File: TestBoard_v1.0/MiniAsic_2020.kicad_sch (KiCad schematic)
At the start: 28 parts, among them J1 Screw_Terminal_01x04, J2 Conn_Coaxial, J3 Conn_Coaxial, J4 Conn_Coaxial, J5 Conn_Coaxial, T1 50@900MHz, T2 50@900MHz, T3 50@900MHz

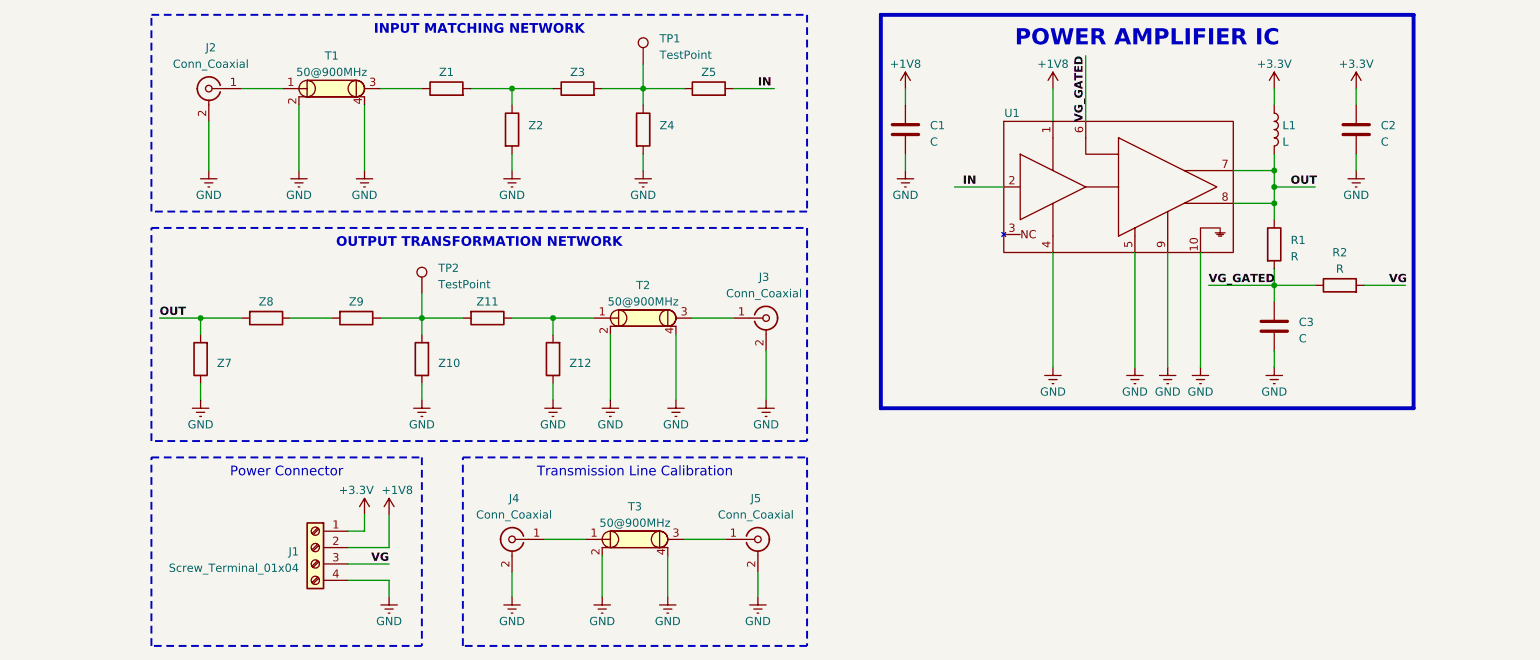
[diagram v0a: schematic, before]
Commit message: Schematic update and initial placement
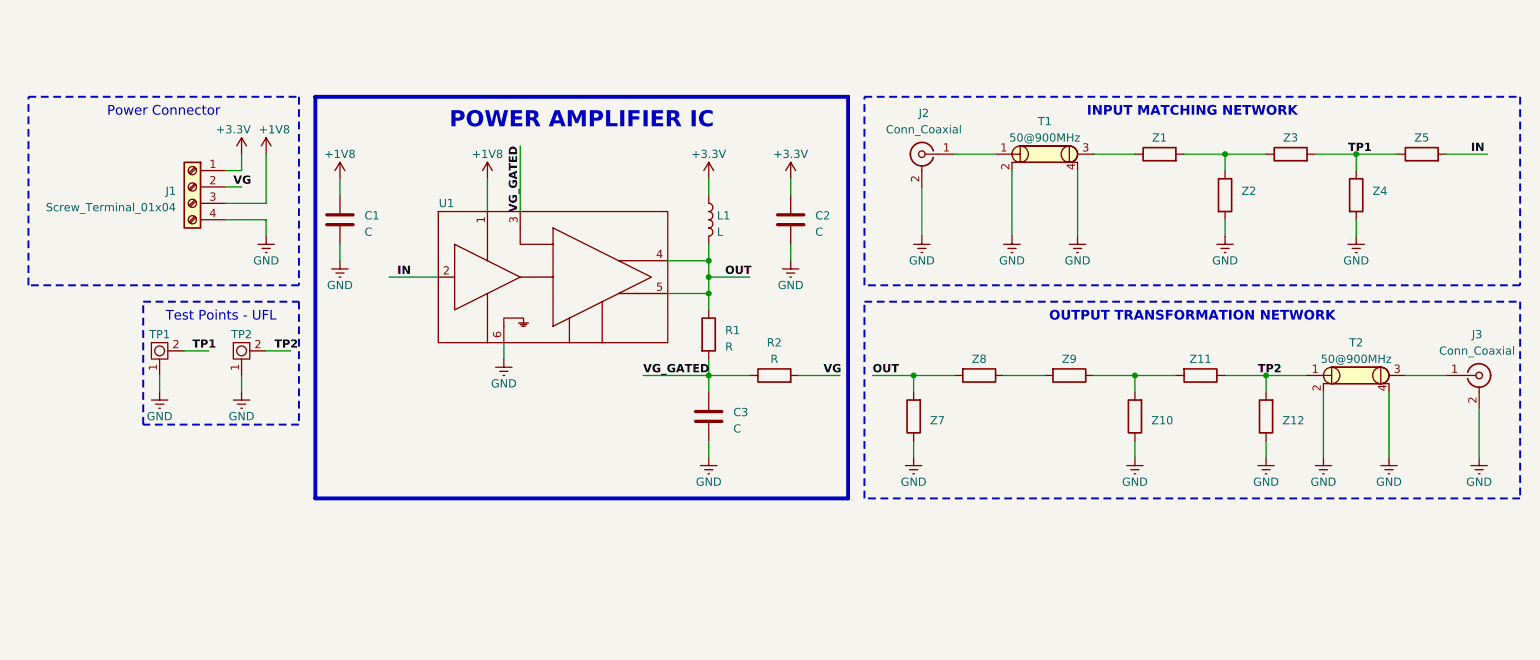
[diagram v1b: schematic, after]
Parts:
- removed J4, J5: Conn_Coaxial, Connector_Coaxial:SMA_Amphenol_901-143_Horizontal, symbol Connector:Conn_Coaxial
- removed T3: 50@900MHz, symbol Simulation_SPICE:TLINE
- removed TP1, TP2: TestPoint, Connector_Coaxial:U.FL_Hirose_U.FL-R-SMT-1_Vertical, symbol Connector:TestPoint
- added TP1, TP2: ~, Connector_Coaxial:U.FL_Hirose_U.FL-R-SMT-1_Vertical, symbol MiniAsic2020_Library_Symbol:TestPoint_UFL
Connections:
- net +1V8: now also J1.3 (Pin_3); no longer J1.2 (Pin_2)
- net OUT: now also U1.4 (OUT_1), U1.5 (OUT_2); no longer U1.7 (OUT_1), U1.8 (OUT_2)
- net VG: now also J1.2 (Pin_2); no longer J1.3 (Pin_3)
- net VG_GATED: now also U1.3 (VG); no longer U1.6 (VG)
- net TP1: now reaches Z3.2, Z4.1, Z5.1
- net TP1: now also TP1.2 (PRB)
- net TP2: now reaches T2.1, Z11.1, Z12.2
- net TP2: now also TP2.2 (PRB)
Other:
- moved on the sheet: C1, C2, C3, J1, J2, J3, L1, R1, R2, T1, T2, Z1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

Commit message: Initial routing
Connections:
- net TP1: now also TP1.1 (PRB); no longer TP1.2 (PRB)
- net TP2: now also TP2.1 (PRB), Z10.2, Z11.2, Z9.1; no longer T2.1, TP2.2 (PRB), Z11.1, Z12.2
- new net: T2.1, Z11.1, Z12.2
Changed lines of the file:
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@@
     (effects (font (size 1.27 1.27) (thickness 0.254) bold) (justify left bottom))
-  )
-  (label "TP2" (at 222.25 106.68 0) (fields_autoplaced)
-    (effects (font (size 1.27 1.27) bold) (justify left bottom))
   )
   (label "TP1" (at 236.22 72.39 0) (fields_autoplaced)
@@
   (label "VG" (at 63.5 77.47 0) (fields_autoplaced)
     (effects (font (size 1.27 1.27) bold) (justify left bottom))
+  )
+  (label "TP2" (at 201.93 106.68 0) (fields_autoplaced)
+    (effects (font (size 1.27 1.27) (thickness 0.254) bold) (justify left bottom))
   )
   (label "IN" (at 255.27 72.39 0) (fields_autoplaced)
@@
     )
   )
-  (symbol (lib_id "MiniAsic2020_Library_Symbol:TestPoint_UFL") (at 52.07 106.68 0) (unit 1)
+  (symbol (lib_name "TestPoint_UFL_1") (lib_id "MiniAsic2020_Library_Symbol:TestPoint_UFL") (at 52.07 106.68 0) (unit 1)
     (in_bom yes) (on_board yes) (dnp no) (fields_autoplaced)
     (property "Reference" "TP1" (at 52.07 100.33 0)

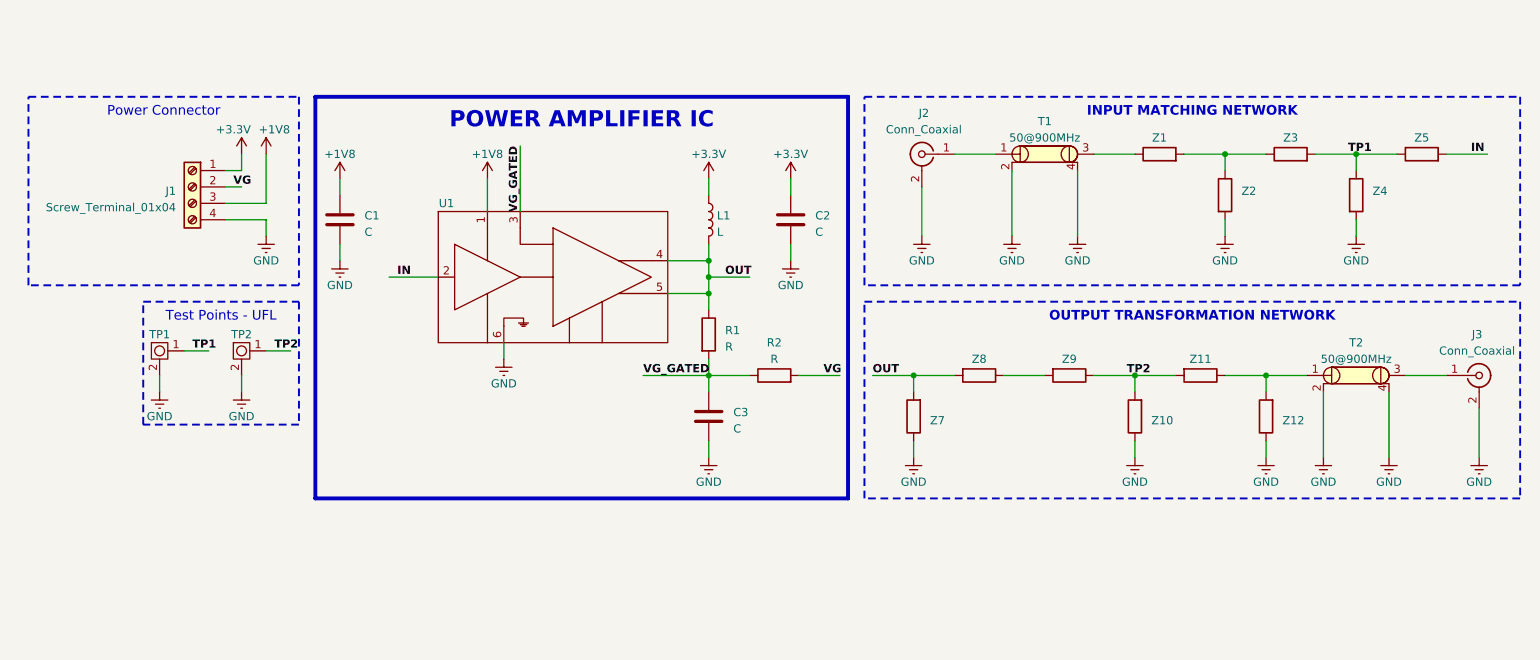
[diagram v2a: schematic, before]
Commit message: New placement focused on the transmission lines
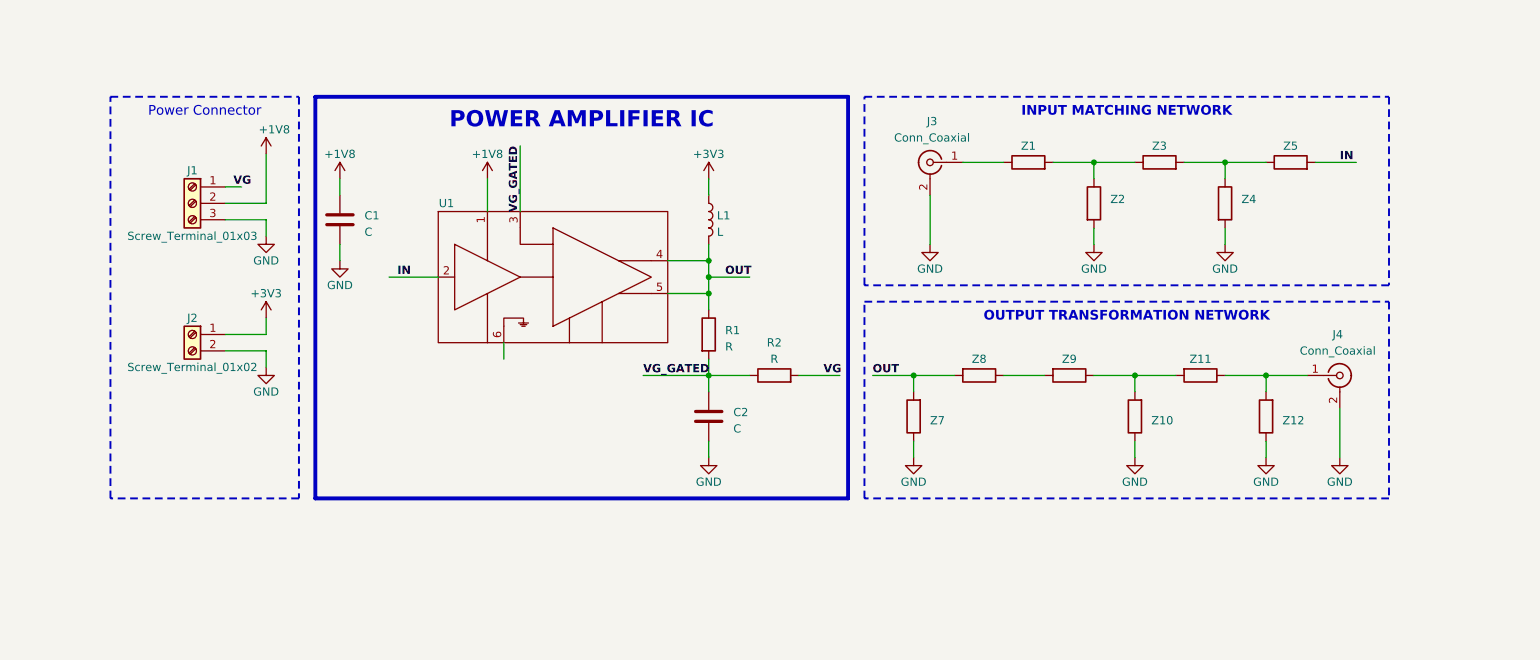
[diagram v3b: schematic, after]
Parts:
- removed C2: C, Capacitor_SMD:C_0603_1608Metric, symbol Device:C
- removed J1: Screw_Terminal_01x04, TerminalBlock:TerminalBlock_bornier-4_P5.08mm, symbol Connector:Screw_Terminal_01x04
- removed T1, T2: 50@900MHz, symbol Simulation_SPICE:TLINE
- removed TP1, TP2: ~, Connector_Coaxial:U.FL_Hirose_U.FL-R-SMT-1_Vertical, symbol MiniAsic2020_Library_Symbol:TestPoint_UFL
- added J1: Screw_Terminal_01x03, TerminalBlock:TerminalBlock_bornier-3_P5.08mm, symbol Connector:Screw_Terminal_01x03
- added J2: Screw_Terminal_01x02, TerminalBlock:TerminalBlock_bornier-2_P5.08mm, symbol Connector:Screw_Terminal_01x02
- renumbered C3 to C2, J2 to J3, J3 to J4
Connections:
- net +1V8: now also J1.2 (Pin_2)
- net VG: now also J1.1 (Pin_1)
- net at J3.1 (In): now also Z1.1
- net GND: now reaches Z2.2
- net GND: now also C1.2, C2.2, J3.2 (Ext), J4.2 (Ext), Z10.1, Z12.1, Z4.2, Z7.1, J1.3 (Pin_3), J2.2 (Pin_2)
- net at J4.1 (In): now also Z11.1, Z12.2
- net +3.3V renamed +3V3
- net +3V3: now also J2.1 (Pin_1)
- net TP1: no longer names the net of Z3.2, Z4.1, Z5.1
- net TP2: no longer names the net of Z10.2, Z11.2, Z9.1
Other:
- moved on the sheet: J3, J4, Z1, Z2, Z3, Z4, Z5

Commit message: Connect IC gnd pad, clean drc, add dimensions, generate gerbers, and export schematic/3d views
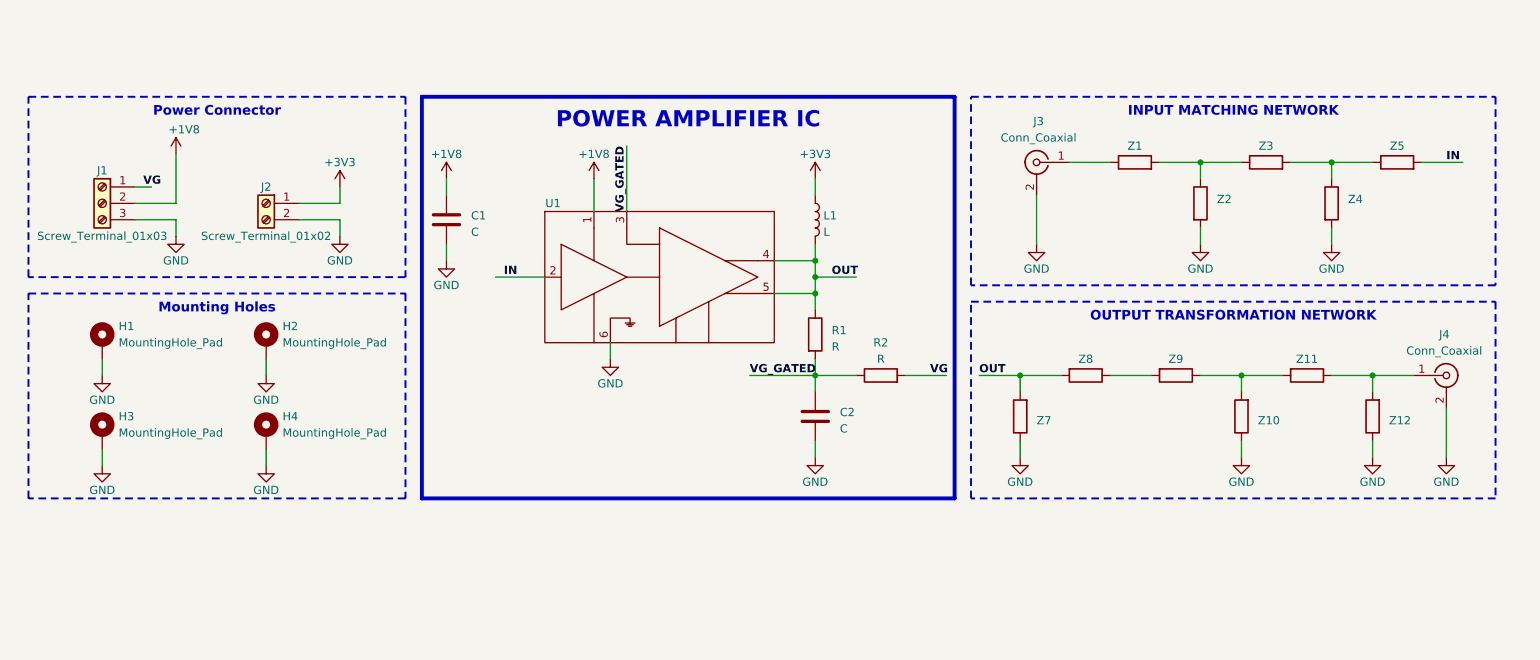
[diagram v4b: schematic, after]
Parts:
- added H1, H2, H3, H4: MountingHole_Pad, MountingHole:MountingHole_3.2mm_M3_Pad_Via, symbol Mechanical:MountingHole_Pad
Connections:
- net GND: now also U1.6 (GND), H1.1, H2.1, H3.1, H4.1
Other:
- moved on the sheet: C1, C2, J1, J2, J3, J4, L1, R1, R2, U1, Z1, Z10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
